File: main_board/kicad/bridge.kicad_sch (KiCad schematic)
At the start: 2 parts, among them Q1 IRFB3077, Q2 IRFB3077

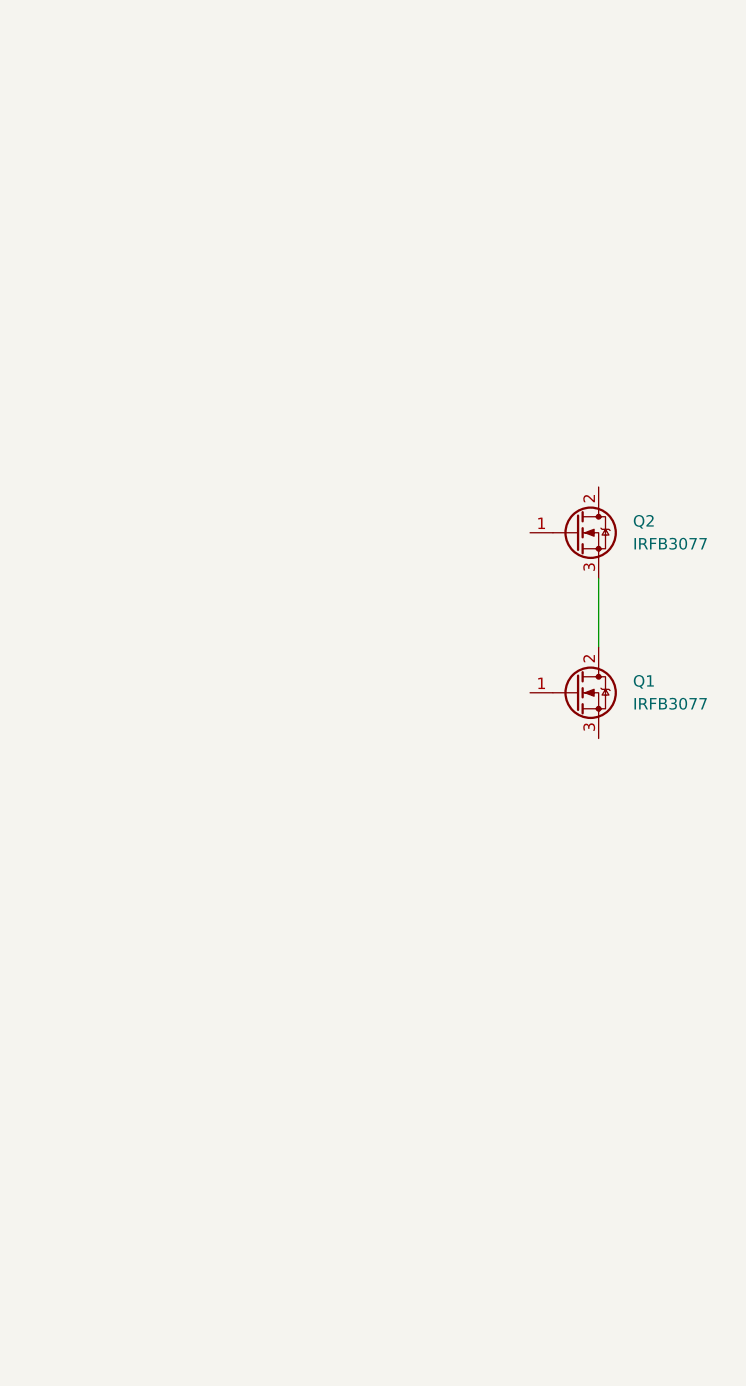
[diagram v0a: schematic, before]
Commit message: changes to bridge design
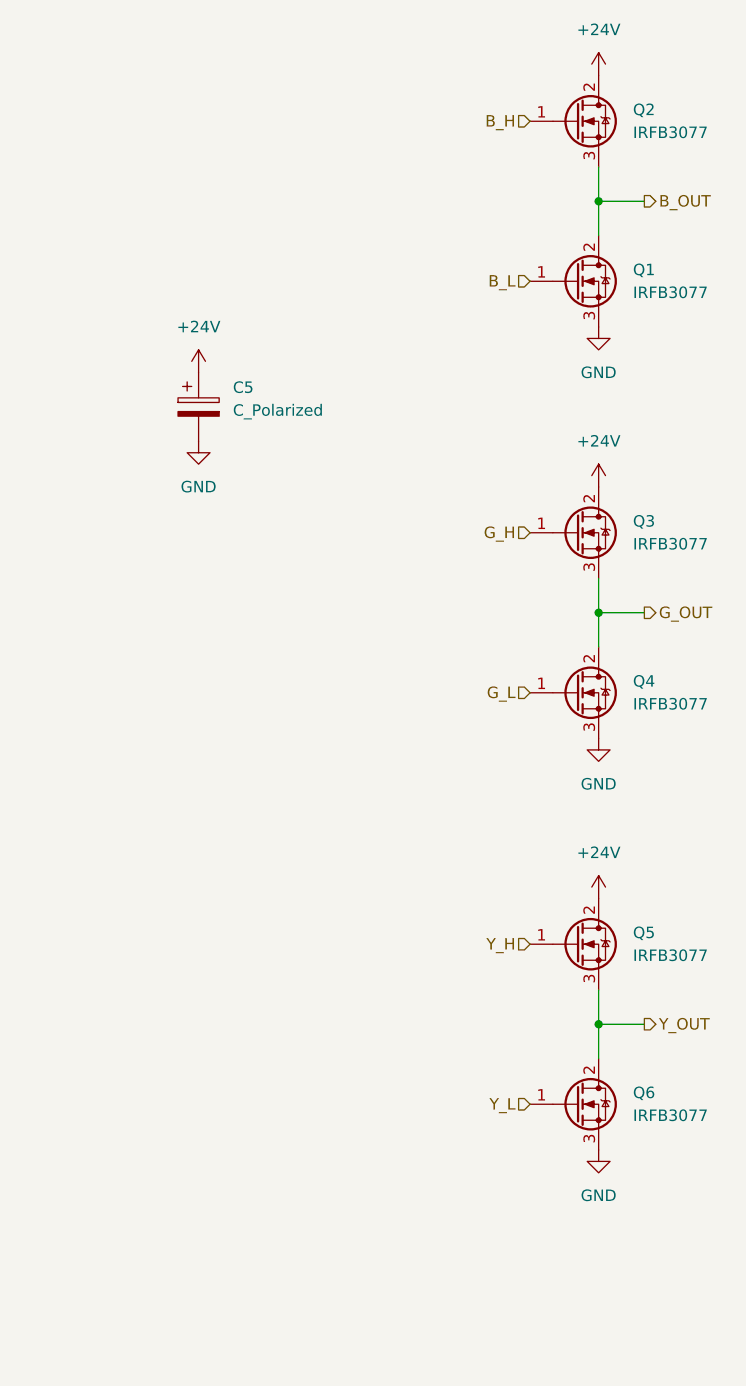
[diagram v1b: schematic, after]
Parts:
- added C5: C_Polarized, symbol Device:C_Polarized
- added Q3, Q4, Q5, Q6: IRFB3077, Package_TO_SOT_THT:TO-220-3_Vertical, symbol 2022-lsd:IRFB3077
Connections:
- net B_L: now reaches Q1.1 (G)
- net B_OUT: now reaches Q1.2 (D), Q2.3 (S)
- net GND: now reaches Q1.3 (S)
- net GND: now also C5.2, Q4.3 (S), Q6.3 (S)
- net B_H: now reaches Q2.1 (G)
- net +24V: now reaches Q2.2 (D)
- net +24V: now also C5.1, Q3.2 (D), Q5.2 (D)
- new net G_H: Q3.1 (G)
- new net G_L: Q4.1 (G)
- new net G_OUT: Q3.3 (S), Q4.2 (D)
- new net Y_H: Q5.1 (G)
- new net Y_L: Q6.1 (G)
- new net Y_OUT: Q5.3 (S), Q6.2 (D)
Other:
- moved on the sheet: Q1, Q2

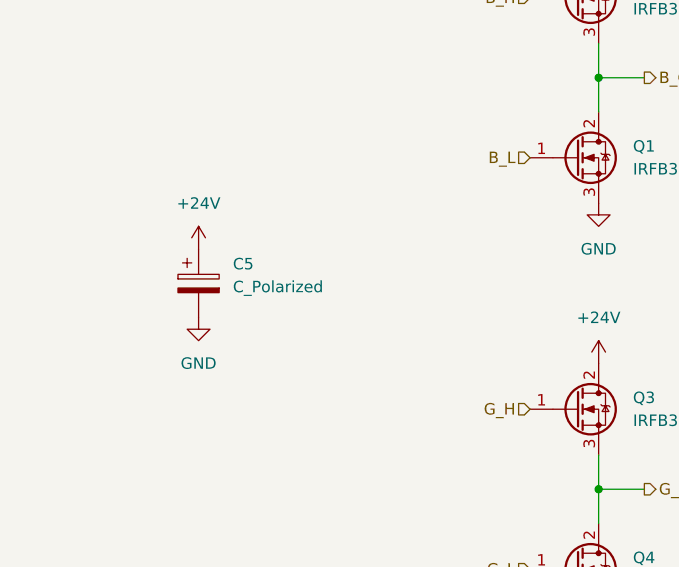
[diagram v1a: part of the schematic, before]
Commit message: implemented 15v stepdown
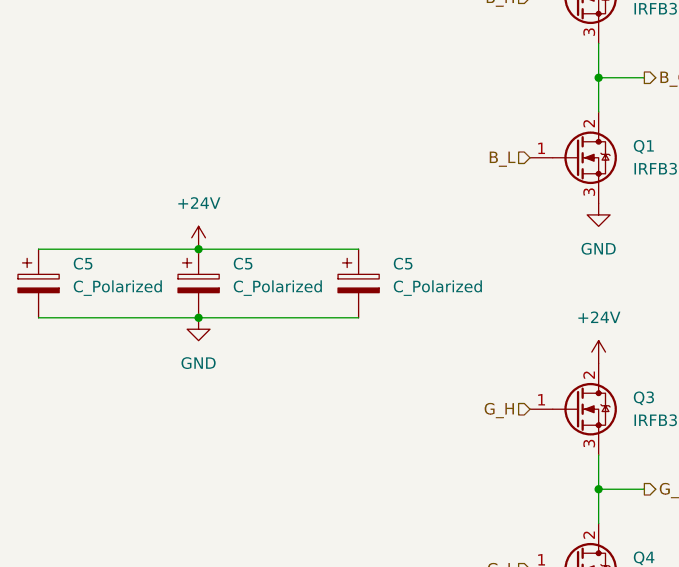
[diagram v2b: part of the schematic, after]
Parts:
- added C5 (x2): C_Polarized, symbol Device:C_Polarized
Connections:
- net +24V: now also C5.1, C5.1
- net GND: now also C5.2, C5.2
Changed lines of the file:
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@@
   (junction (at 116.84 90.17) (diameter 0) (color 0 0 0 0)
   )
+  (junction (at 72.39 71.12) (diameter 0) (color 0 0 0 0)
+  )
+  (junction (at 72.39 63.5) (diameter 0) (color 0 0 0 0)
+  )
   (junction (at 116.84 44.45) (diameter 0) (color 0 0 0 0)
   )
@@
     (stroke (width 0) (type default))
   )
+  (wire (pts (xy 72.39 71.12) (xy 90.17 71.12))
+    (stroke (width 0) (type default))
+  )
+  (wire (pts (xy 72.39 63.5) (xy 90.17 63.5))
+    (stroke (width 0) (type default))
+  )
   (wire (pts (xy 116.84 132.08) (xy 116.84 135.89))
     (stroke (width 0) (type default))
   )
+  (wire (pts (xy 54.61 63.5) (xy 72.39 63.5))
+    (stroke (width 0) (type default))
+  )
   (wire (pts (xy 116.84 135.89) (xy 116.84 139.7))
     (stroke (width 0) (type default))
   )
   (wire (pts (xy 116.84 44.45) (xy 121.92 44.45))
+    (stroke (width 0) (type default))
+  )
+  (wire (pts (xy 54.61 71.12) (xy 72.39 71.12))
     (stroke (width 0) (type default))
   )
@@
     )
   )
+  (symbol (lib_id "Device:C_Polarized") (at 90.17 67.31 0) (unit 1)
+    (in_bom yes) (on_board yes) (dnp no) (fields_autoplaced)
+    (property "Reference" "C5" (at 93.98 65.151 0)
+      (effects (font (size 1.27 1.27)) (justify left))
+    )
+    (property "Value" "C_Polarized" (at 93.98 67.691 0)
+      (effects (font (size 1.27 1.27)) (justify left))
+    )
+    (property "Footprint" "" (at 91.1352 71.12 0)
+      (effects (font (size 1.27 1.27)) hide)
+    )
+    (property "Datasheet" "~" (at 90.17 67.31 0)
+      (effects (font (size 1.27 1.27)) hide)
+    )
+    (pin "1")
+    (pin "2")
+    (instances
+      (project "main"
+        (path "/9139d8e7-a5dc-421f-9a12-f77d83384a16"
+          (reference "C5") (unit 1)
+        )
+        (path "/9139d8e7-a5dc-421f-9a12-f77d83384a16/2bccd4f1-b739-4e07-a189-131f62508a72"
+          (reference "C14") (unit 1)
+        )
+      )
+    )
+  )
   (symbol (lib_id "power:+24V") (at 116.84 121.92 0) (unit 1)
     (in_bom yes) (on_board yes) (dnp no) (fields_autoplaced)
@@
         )
       )
+    )
+  )
+  (symbol (lib_id "Device:C_Polarized") (at 54.61 67.31 0) (unit 1)
+    (in_bom yes) (on_board yes) (dnp no) (fields_autoplaced)
+    (property "Reference" "C5" (at 58.42 65.151 0)
+      (effects (font (size 1.27 1.27)) (justify left))
+    )
+    (property "Value" "C_Polarized" (at 58.42 67.691 0)
+      (effects (font (size 1.27 1.27)) (justify left))
+    )
+    (property "Footprint" "" (at 55.5752 71.12 0)
+      (effects (font (size 1.27 1.27)) hide)
+    )
+    (property "Datasheet" "~" (at 54.61 67.31 0)
+      (effects (font (size 1.27 1.27)) hide)
+    )
+    (pin "1")
+    (pin "2")
+    (instances
+      (project "main"
+        (path "/9139d8e7-a5dc-421f-9a12-f77d83384a16"
+          (reference "C5") (unit 1)
+        )
+        (path "/9139d8e7-a5dc-421f-9a12-f77d83384a16/2bccd4f1-b739-4e07-a189-131f62508a72"
+          (reference "C13") (unit 1)
+        )
+      )

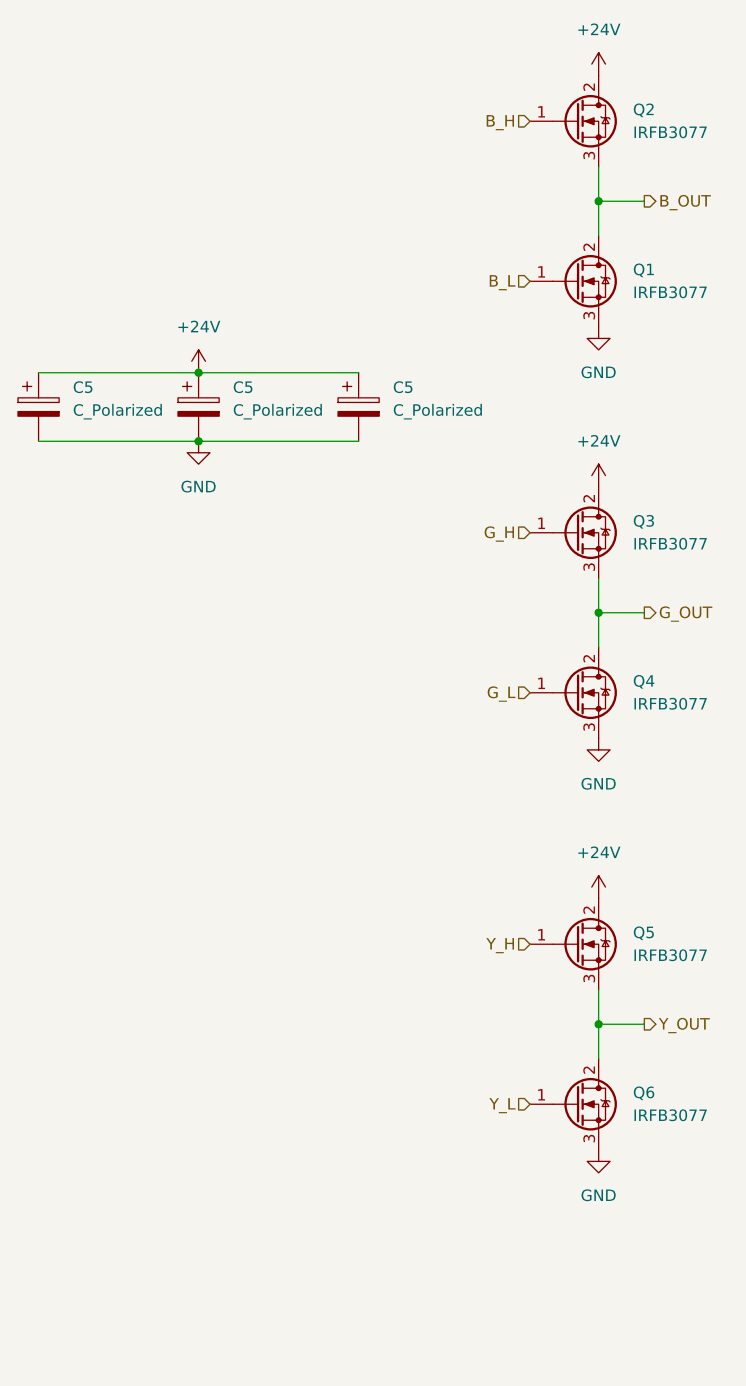
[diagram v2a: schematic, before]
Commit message: added cancel diodes and pullup to bridge
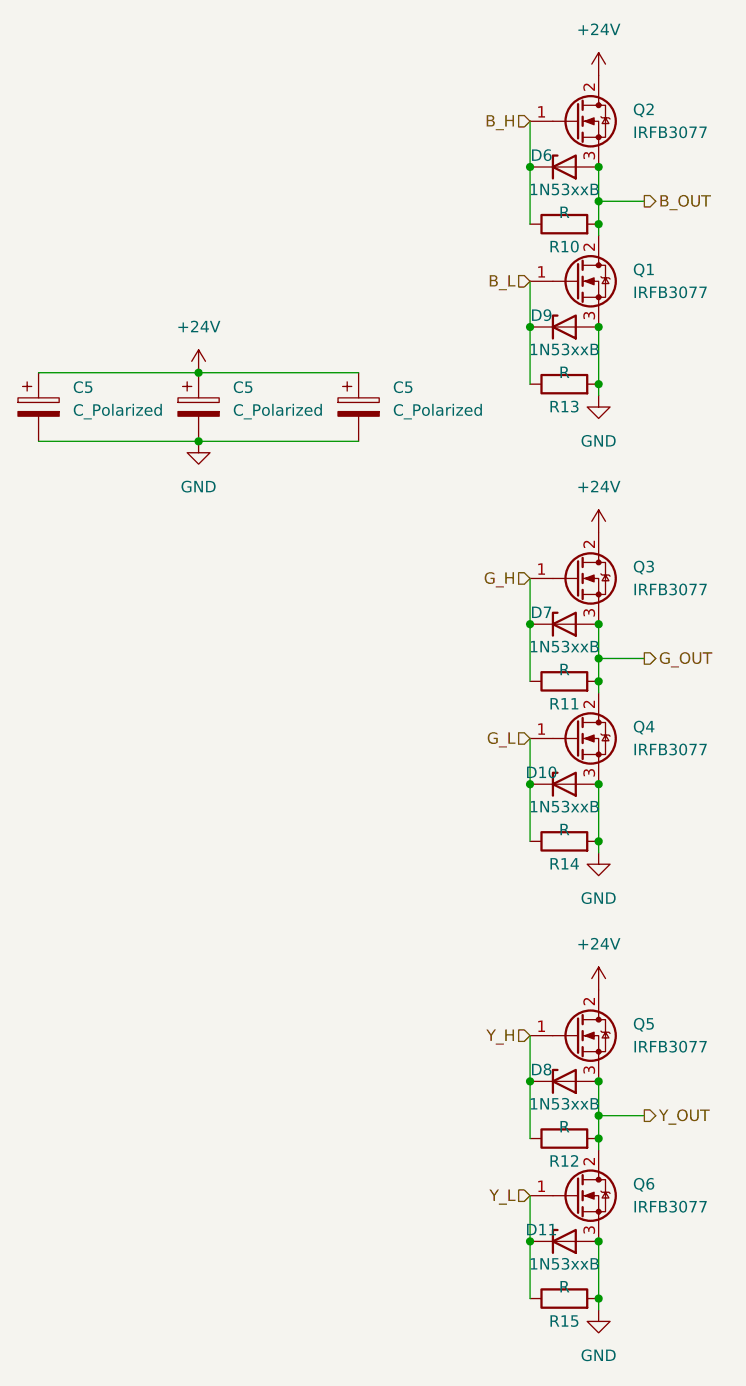
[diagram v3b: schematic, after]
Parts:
- added D10, D11, D6, D7, D8, D9: 1N53xxB, Diode_THT:D_DO-201_P15.24mm_Horizontal, symbol Diode:1N53xxB
- added R10, R11, R12, R13, R14, R15: R, symbol Device:R
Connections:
- net B_H: now also D6.1 (K), R10.1
- net B_L: now also D9.1 (K), R13.1
- net B_OUT: now also D6.2 (A), R10.2
- net GND: now also D10.2 (A), D11.2 (A), D9.2 (A), R13.2, R14.2, R15.2
- net G_H: now also D7.1 (K), R11.1
- net G_L: now also D10.1 (K), R14.1
- net G_OUT: now also D7.2 (A), R11.2
- net Y_H: now also D8.1 (K), R12.1
- net Y_L: now also D11.1 (K), R15.1
- net Y_OUT: now also D8.2 (A), R12.2
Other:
- moved on the sheet: Q3, Q4, Q5, Q6
